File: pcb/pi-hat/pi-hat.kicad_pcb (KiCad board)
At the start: 2 copper layers, 65 x 27.6 mm, 20 parts, among them IC3 THVD1420DR, IC4 THVD1420DR, J1 GPIO, J2 RJ45

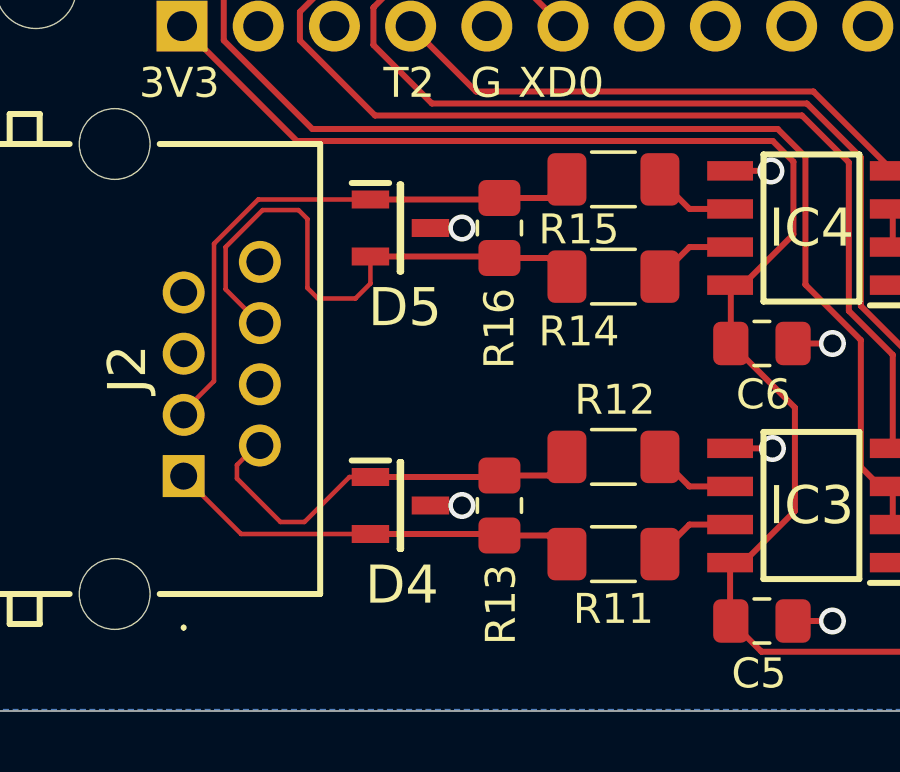
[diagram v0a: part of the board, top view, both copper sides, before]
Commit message: Several changes while testing.
Primary is that 5v was being used as the power rail when 3V3 was needed on the Pi hat and row controller board, where the RPi5 and RP2350 are both 3V3 logic.  On the Pi Hat a second UART to RS-485 was also added to have dual buses, enabling 6.25 Gbps, given the RPi5 is limited to 3.125Mbps
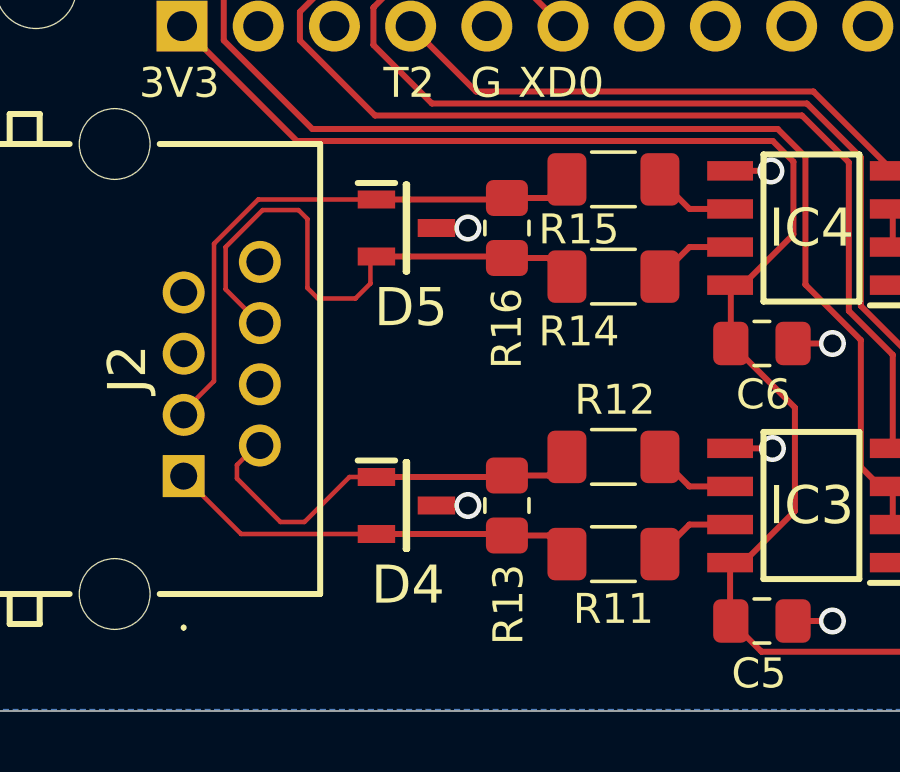
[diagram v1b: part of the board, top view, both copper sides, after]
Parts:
- moved R13 0.25 mm to (119.2, 64.8)
- moved R16 0.25 mm to (119.2, 55.5)
- moved D4 0.20 mm to (115.8, 64.8)
- moved D5 0.20 mm to (115.8, 55.5)
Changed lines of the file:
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@@
 	(footprint "Resistor_SMD:R_0805_2012Metric_Pad1.20x1.40mm_HandSolder"
 		(layer "F.Cu")
-		(at 118.95 64.75 -90)
+		(at 119.2 64.75 -90)
 		(descr "Resistor SMD 0805 (2012 Metric), square (rectangular) end terminal, IPC-7351 nominal with elongated pad for handsoldering. (Body size source: IPC-SM-782 page 72, https://www.pcb-3d.com/wordpress/wp-content/uploads/ipc-sm-782a_amendment_1_and_2.pdf)")
 		(tags "resistor handsolder")
@@
 	(footprint "Garth:SOT95P230X117-3N"
 		(layer "F.Cu")
-		(at 115.65 55.5)
+		(at 115.85 55.5)
 		(descr "sot-23-sm")
 		(tags "Diode")
@@
 	(footprint "Resistor_SMD:R_0805_2012Metric_Pad1.20x1.40mm_HandSolder"
 		(layer "F.Cu")
-		(at 118.95 55.5 -90)
+		(at 119.2 55.5 -90)
 		(descr "Resistor SMD 0805 (2012 Metric), square (rectangular) end terminal, IPC-7351 nominal with elongated pad for handsoldering. (Body size source: IPC-SM-782 page 72, https://www.pcb-3d.com/wordpress/wp-content/uploads/ipc-sm-782a_amendment_1_and_2.pdf)")
 		(tags "resistor handsolder")
@@
 	(footprint "Garth:SOT95P230X117-3N"
 		(layer "F.Cu")
-		(at 115.65 64.75)
+		(at 115.85 64.75)
 		(descr "sot-23-sm")
 		(tags "Diode")
@@
 	)
 	(via
-		(at 117.7 55.5)
+		(at 117.9 55.5)
 		(size 0.9)
 		(drill 0.6)
@@
 	)
 	(via
-		(at 117.7 64.75)
+		(at 117.9 64.75)
 		(size 0.9)
 		(drill 0.6)
@@
 	)
 	(segment
-		(start 118.95 63.75)
-		(end 120.58 63.75)
+		(start 119.15 63.8)
+		(end 119.2 63.75)
 		(width 0.2)
 		(layer "F.Cu")
@@
 	)
 	(segment
+		(start 119.2 63.75)
+		(end 120.58 63.75)
+		(width 0.2)
+		(layer "F.Cu")
+		(net "/orange_A")
+	)
+	(segment
 		(start 110.2 63.85)
 		(end 110.2 63.4)
@@
 	)
 	(segment
-		(start 114.65 63.8)
-		(end 118.9 63.8)
-		(width 0.2)
-		(layer "F.Cu")
-		(net "/orange_A")
-	)
-	(segment
 		(start 110.2 63.4)
 		(end 110.9 62.7)
@@
 	)
 	(segment
+		(start 114.85 63.8)
+		(end 119.15 63.8)
+		(width 0.2)
+		(layer "F.Cu")
+		(net "/orange_A")
+	)
+	(segment
 		(start 120.58 63.75)
 		(end 121.2 63.13)
@@
 	)
 	(segment
-		(start 118.9 65.7)
-		(end 118.95 65.75)
+		(start 119.2 65.75)
+		(end 120.58 65.75)
 		(width 0.2)
 		(layer "F.Cu")
@@
 	)
 	(segment
-		(start 108.36 63.72)
-		(end 110.34 65.7)
-		(width 0.1524)
+		(start 118.9 65.7)
+		(end 118.95 65.75)
+		(width 0.2)
 		(layer "F.Cu")
 		(net "/orange_B")
 	)
 	(segment
-		(start 114.65 65.7)
-		(end 118.9 65.7)
+		(start 119.15 65.7)
+		(end 119.2 65.75)
 		(width 0.2)
 		(layer "F.Cu")
@@
 	)
 	(segment
-		(start 118.95 65.75)
-		(end 120.58 65.75)
+		(start 114.85 65.7)
+		(end 119.15 65.7)
 		(width 0.2)
 		(layer "F.Cu")
 		(net "/orange_B")
+	)
+	(segment
+		(start 108.36 63.72)
+		(end 110.34 65.7)
+		(width 0.1524)
+		(layer "F.Cu")
+		(net "/orange_B")
